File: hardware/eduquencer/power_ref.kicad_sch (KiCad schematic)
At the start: 23 parts

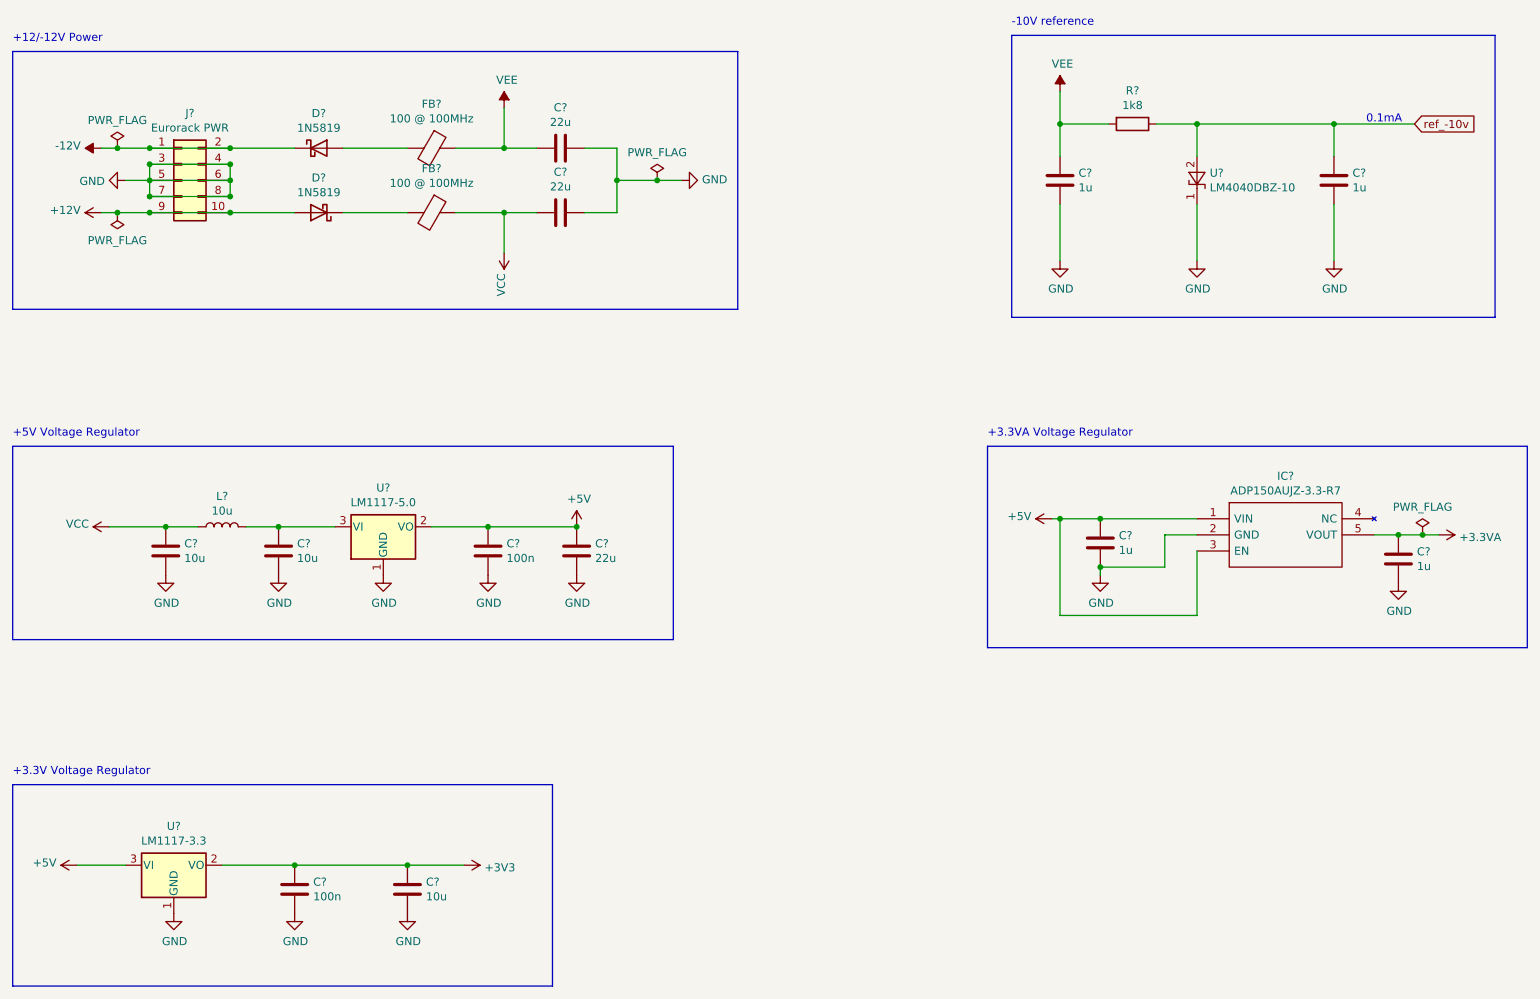
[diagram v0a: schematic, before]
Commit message: add 5/10V voltage references
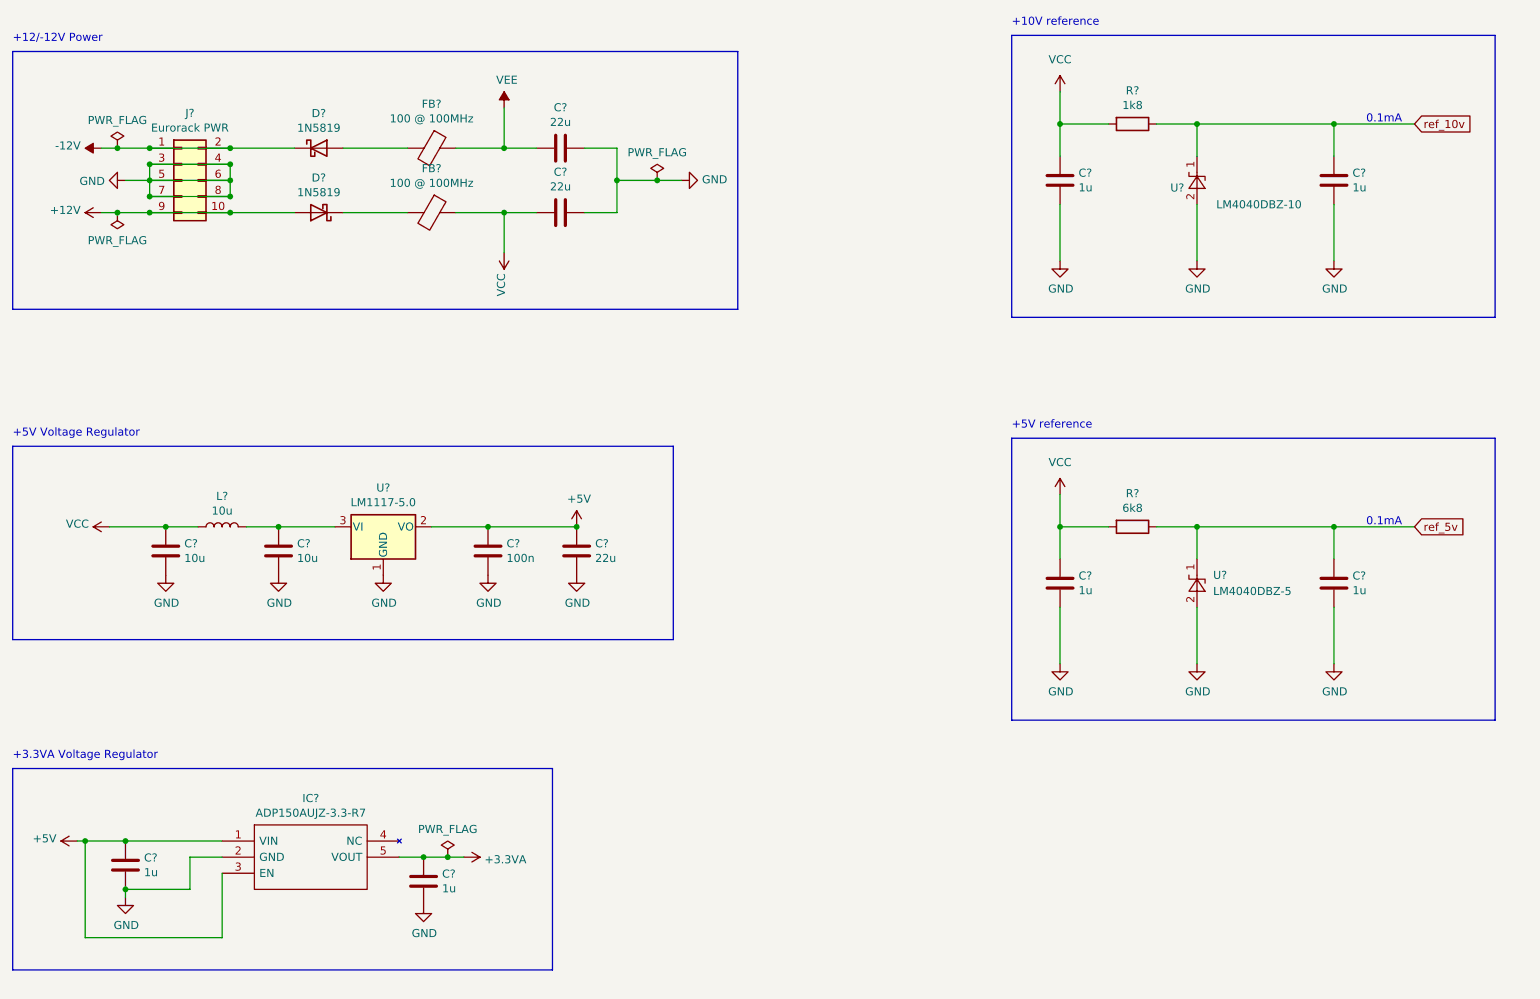
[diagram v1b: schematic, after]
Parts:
- removed C?: 100n, Capacitor_SMD:C_0603_1608Metric, symbol Device:C
- removed C?: 10u, Capacitor_SMD:C_0805_2012Metric, symbol Device:C
- removed U?: LM1117-3.3, Package_TO_SOT_SMD:SOT-223, symbol Regulator_Linear:LM1117-3.3
- added C? (x2): 1u, Capacitor_SMD:C_0603_1608Metric, symbol Device:C
- added R?: 6k8, Resistor_SMD:R_0603_1608Metric, symbol Device:R
- added U?: LM4040DBZ-5, Package_TO_SOT_SMD:SOT-23, symbol Reference_Voltage:LM4040DBZ-5
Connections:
- net GND: now also U?.2 (A), C?.2, C?.2, U?.2 (A); no longer U?.1 (K)
- net VCC: now also C?.1, R?.2, C?.1, R?.2
- net VEE: no longer C?.1, R?.2
- net ref_-10v renamed ref_10v
- net ref_10v: now also U?.1 (K); no longer U?.2 (A)
- new net ref_5v: C?.1, R?.1, U?.1 (K)
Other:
- note added: "+10V reference"
- note added: "+5V reference"
- note removed: "+3.3V Voltage Regulator"
- note removed: "-10V reference"
- moved on the sheet: C?, IC?, U?

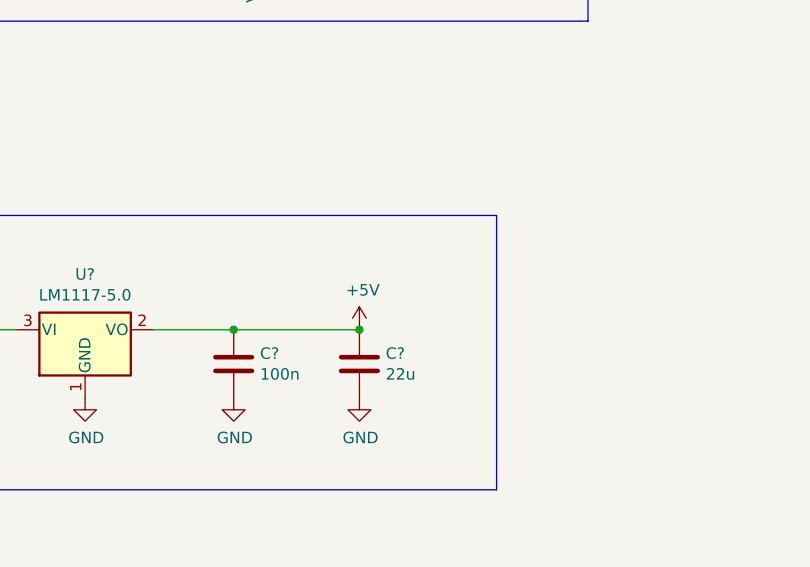
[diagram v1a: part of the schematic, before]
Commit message: Hardware: add trigger in&outputs, wire rpi
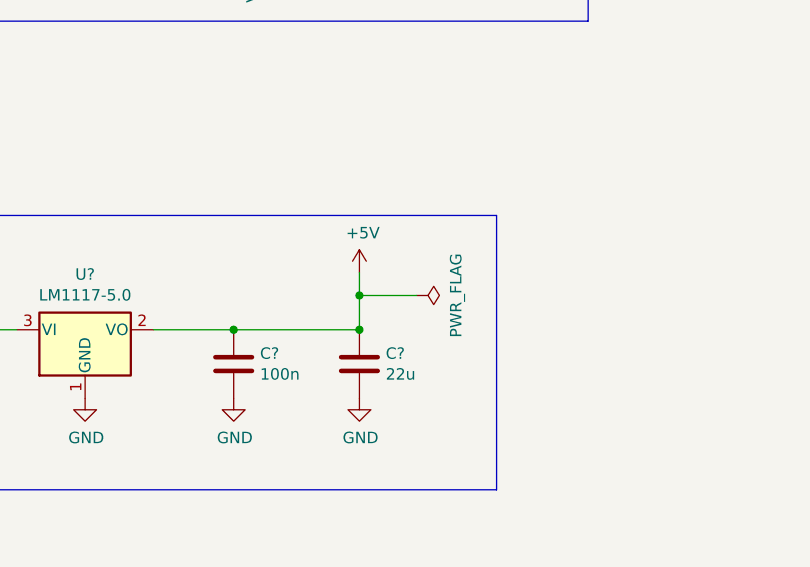
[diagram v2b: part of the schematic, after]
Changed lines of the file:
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@@
   (junction (at 46.99 53.34) (diameter 0) (color 0 0 0 0)
   )
+  (junction (at 114.3 102.87) (diameter 0) (color 0 0 0 0)
+  )
+  (junction (at 114.3 99.06) (diameter 0) (color 0 0 0 0)
+  )
   (junction (at 100.33 102.87) (diameter 0) (color 0 0 0 0)
   )
@@
   (junction (at 46.99 48.26) (diameter 0) (color 0 0 0 0)
   )
-  (junction (at 114.3 102.87) (diameter 0) (color 0 0 0 0)
-  )
   (junction (at 43.18 152.4) (diameter 0) (color 0 0 0 0)
   )
@@
     (stroke (width 0) (type default) (color 0 0 0 0))
   )
+  (wire (pts (xy 114.3 96.52) (xy 114.3 99.06))
+    (stroke (width 0) (type default) (color 0 0 0 0))
+  )
   (wire (pts (xy 212.09 102.87) (xy 212.09 107.95))
     (stroke (width 0) (type default) (color 0 0 0 0))
@@
     (stroke (width 0) (type default) (color 0 0 0 0))
   )
+  (wire (pts (xy 114.3 99.06) (xy 114.3 102.87))
+    (stroke (width 0) (type default) (color 0 0 0 0))
+  )
   (wire (pts (xy 212.09 102.87) (xy 233.68 102.87))
     (stroke (width 0) (type default) (color 0 0 0 0))
@@
   )
   (polyline (pts (xy 25.4 68.58) (xy 139.7 68.58))
+    (stroke (width 0) (type default) (color 0 0 0 0))
+  )
+  (wire (pts (xy 114.3 99.06) (xy 120.65 99.06))
     (stroke (width 0) (type default) (color 0 0 0 0))
   )
@@
     (pin "2")
   )
-  (symbol (lib_id "power:+5V") (at 114.3 102.87 0) (unit 1)
-    (in_bom yes) (on_board yes)
-    (property "Reference" "#PWR?" (id 0) (at 114.3 106.68 0)
-      (effects (font (size 1.27 1.27)) hide)
-    )
-    (property "Value" "+5V" (id 1) (at 114.681 98.4758 0))
-    (property "Footprint" "" (id 2) (at 114.3 102.87 0)
-      (effects (font (size 1.27 1.27)) hide)
-    )
-    (property "Datasheet" "" (id 3) (at 114.3 102.87 0)
+  (symbol (lib_id "power:+5V") (at 114.3 96.52 0) (unit 1)
+    (in_bom yes) (on_board yes)
+    (property "Reference" "#PWR?" (id 0) (at 114.3 100.33 0)
+      (effects (font (size 1.27 1.27)) hide)
+    )
+    (property "Value" "+5V" (id 1) (at 114.681 92.1258 0))
+    (property "Footprint" "" (id 2) (at 114.3 96.52 0)
+      (effects (font (size 1.27 1.27)) hide)
+    )
+    (property "Datasheet" "" (id 3) (at 114.3 96.52 0)
       (effects (font (size 1.27 1.27)) hide)
     )
@@
     (pin "2")
   )
+  (symbol (lib_id "power:PWR_FLAG") (at 120.65 99.06 270) (unit 1)
+    (in_bom yes) (on_board yes)
+    (property "Reference" "#FLG?" (id 0) (at 122.555 99.06 0)
+      (effects (font (size 1.27 1.27)) hide)
+    )
+    (property "Value" "PWR_FLAG" (id 1) (at 125.0442 99.06 0))
+    (property "Footprint" "" (id 2) (at 120.65 99.06 0)
+      (effects (font (size 1.27 1.27)) hide)
+    )
+    (property "Datasheet" "~" (id 3) (at 120.65 99.06 0)
+      (effects (font (size 1.27 1.27)) hide)
+    )
+    (pin "1")
+  )
   (symbol (lib_id "power:GND") (at 212.09 124.46 0) (unit 1)

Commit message: Hardware: add test points, tiny cleanup
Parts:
- C? (x6): LCSC C15849 -> (none); LCSC Part # C15849 -> (none)
- C?: LCSC C45783 -> (none); LCSC Part # C45783 -> (none)
- C? (x2): LCSC C15850 -> (none); LCSC Part # C15850 -> (none)
- C?: LCSC C14663 -> (none); LCSC Part # C14663 -> (none)
- C? (x2): LCSC C249700 -> (none); LCSC Part # C249700 -> (none)
- D? (x2): LCSC C8598 -> (none); LCSC Part # C8598 -> (none)
- FB? (x2): LCSC C1015 -> (none); LCSC Part # C1015 -> (none)
- IC?: LCSC C29149 -> (none); LCSC Part # C29149 -> (none)
- L?: LCSC C1035 -> (none); LCSC Part # C1035 -> (none)
- R? (x2): LCSC C4177 -> (none); LCSC Part # C4177 -> (none)
- U?: LCSC C201738 -> (none); LCSC Part # C201738 -> (none)
- U?: LCSC C6187 -> (none); LCSC Part # C6187 -> (none)
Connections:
- net GND: no longer C?.2, C?.2, IC?.2 (GND)
- new net GNDA: C?.2, C?.2, IC?.2 (GND)

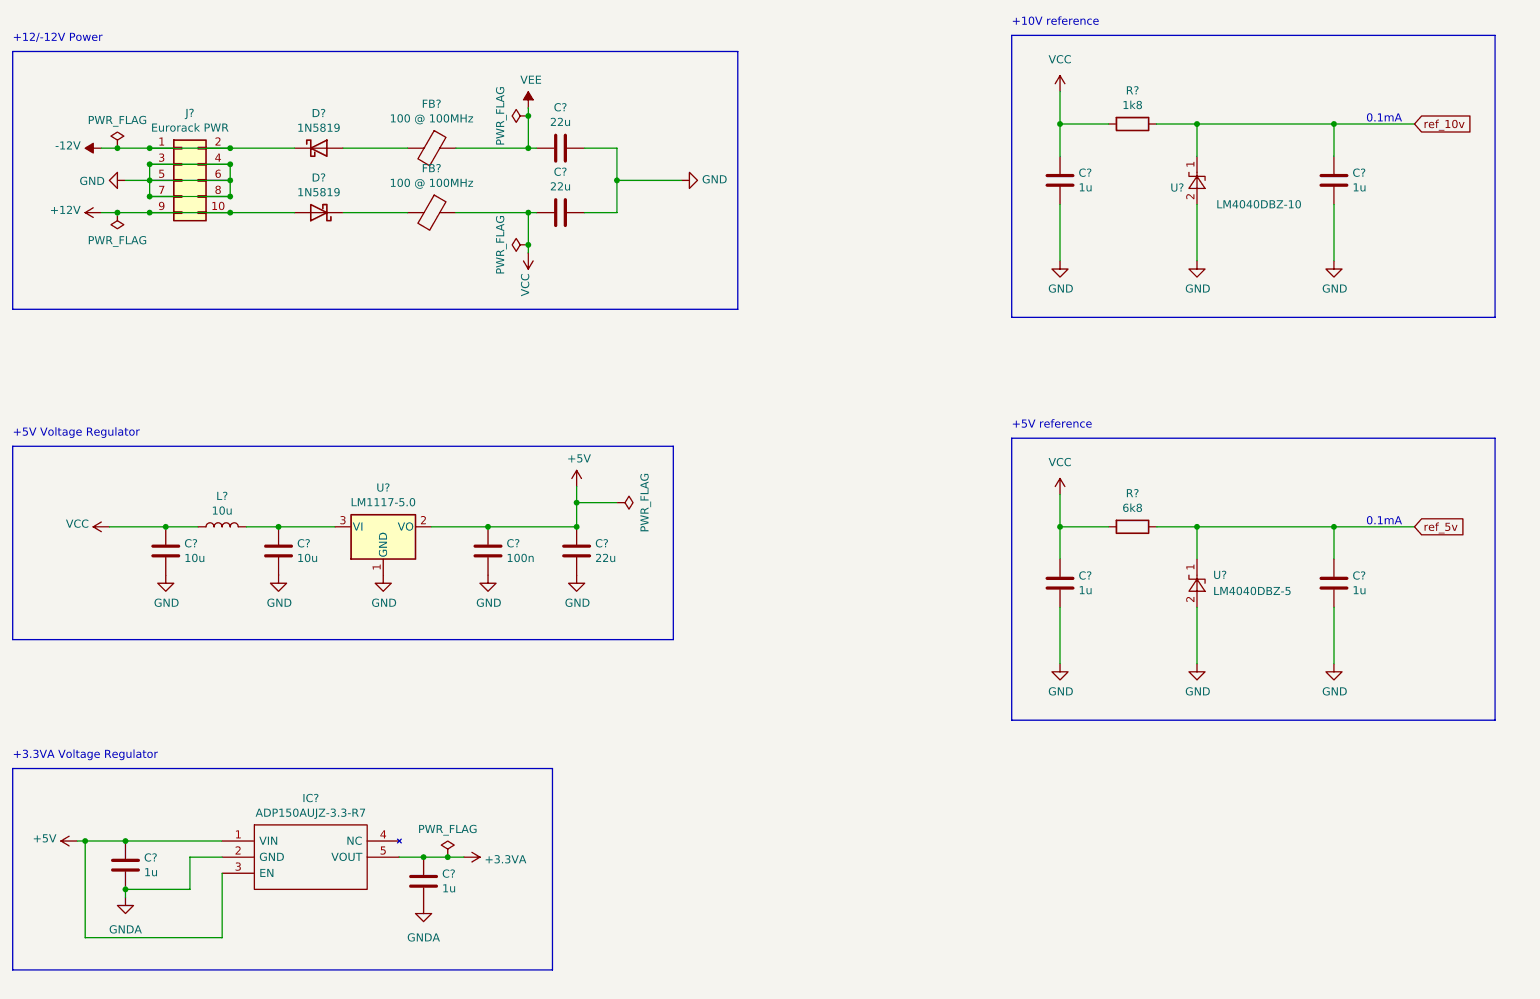
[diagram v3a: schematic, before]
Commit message: Hardware: update models, annotate, fix ERC issues
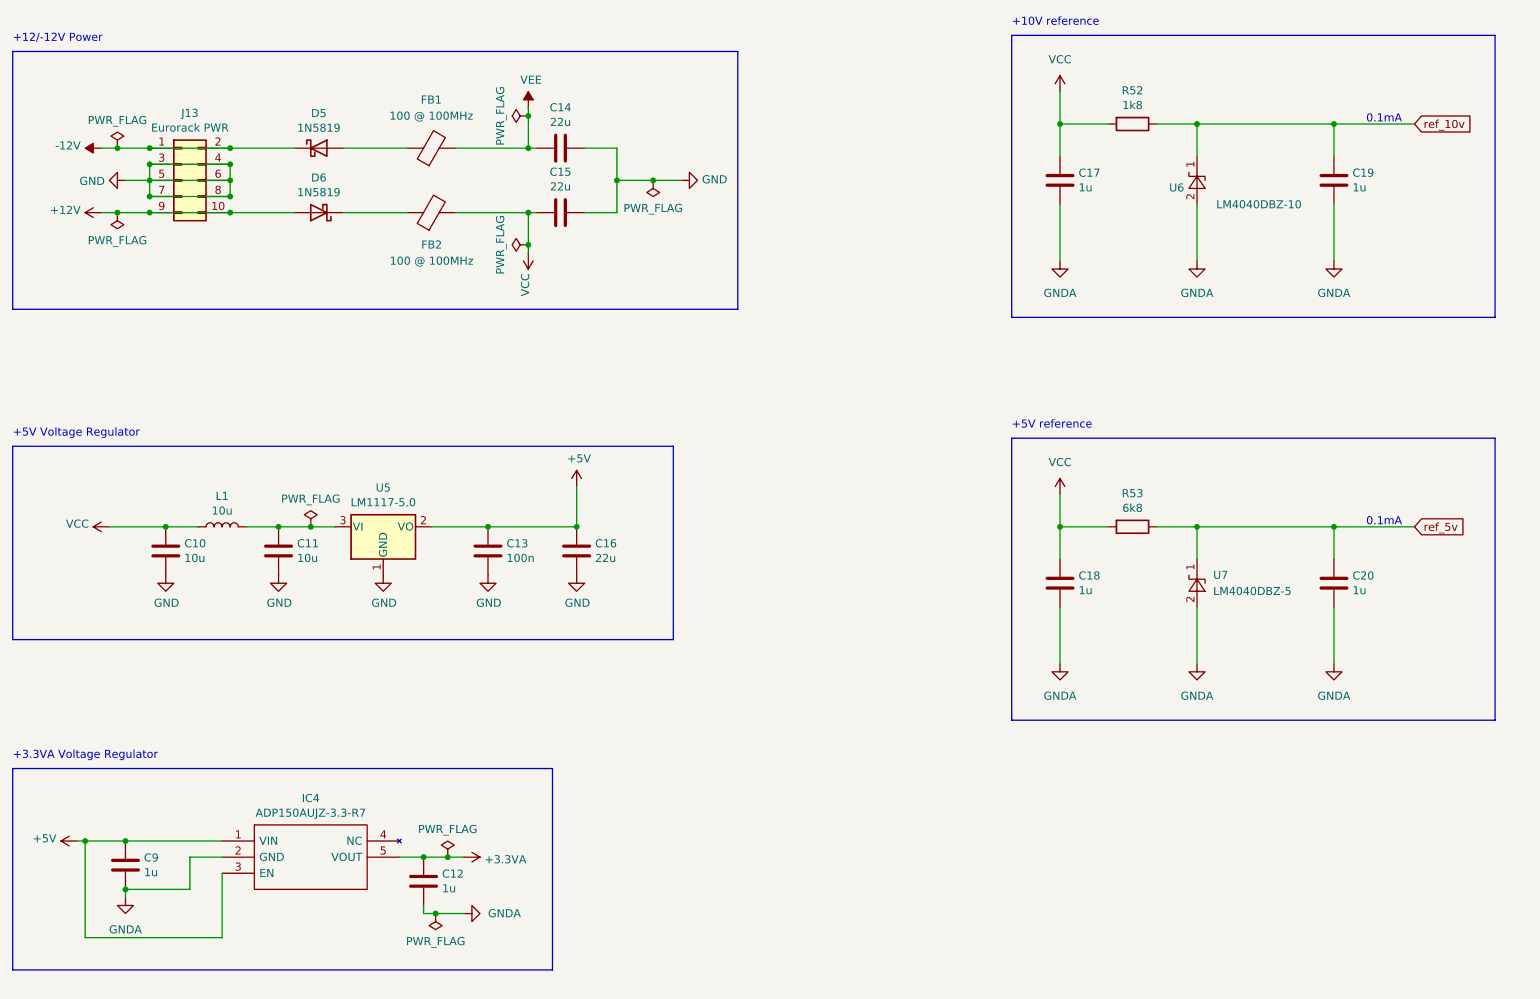
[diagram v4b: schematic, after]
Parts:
- removed FB? (x2): 100 @ 100MHz, Inductor_SMD:L_0805_2012Metric, symbol Device:Ferrite_Bead
- added FB1, FB2: 100 @ 100MHz, Inductor_SMD:L_0805_2012Metric_Pad1.05x1.20mm_HandSolder, symbol Device:FerriteBead
- gave numbers to parts that had none: 22
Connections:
- net GND: no longer C17.2, C18.2, C19.2, C20.2, U6.2 (A), U7.2 (A)
- net GNDA: now also C17.2, C18.2, C19.2, C20.2, U6.2 (A), U7.2 (A)
- net VCC: now also FB2.2
- net VEE: now also FB1.2
- net at D6.1 (K): now also FB2.1
- net at D5.2 (A): now also FB1.1
